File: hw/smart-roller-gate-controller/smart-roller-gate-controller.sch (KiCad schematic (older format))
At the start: 6 parts

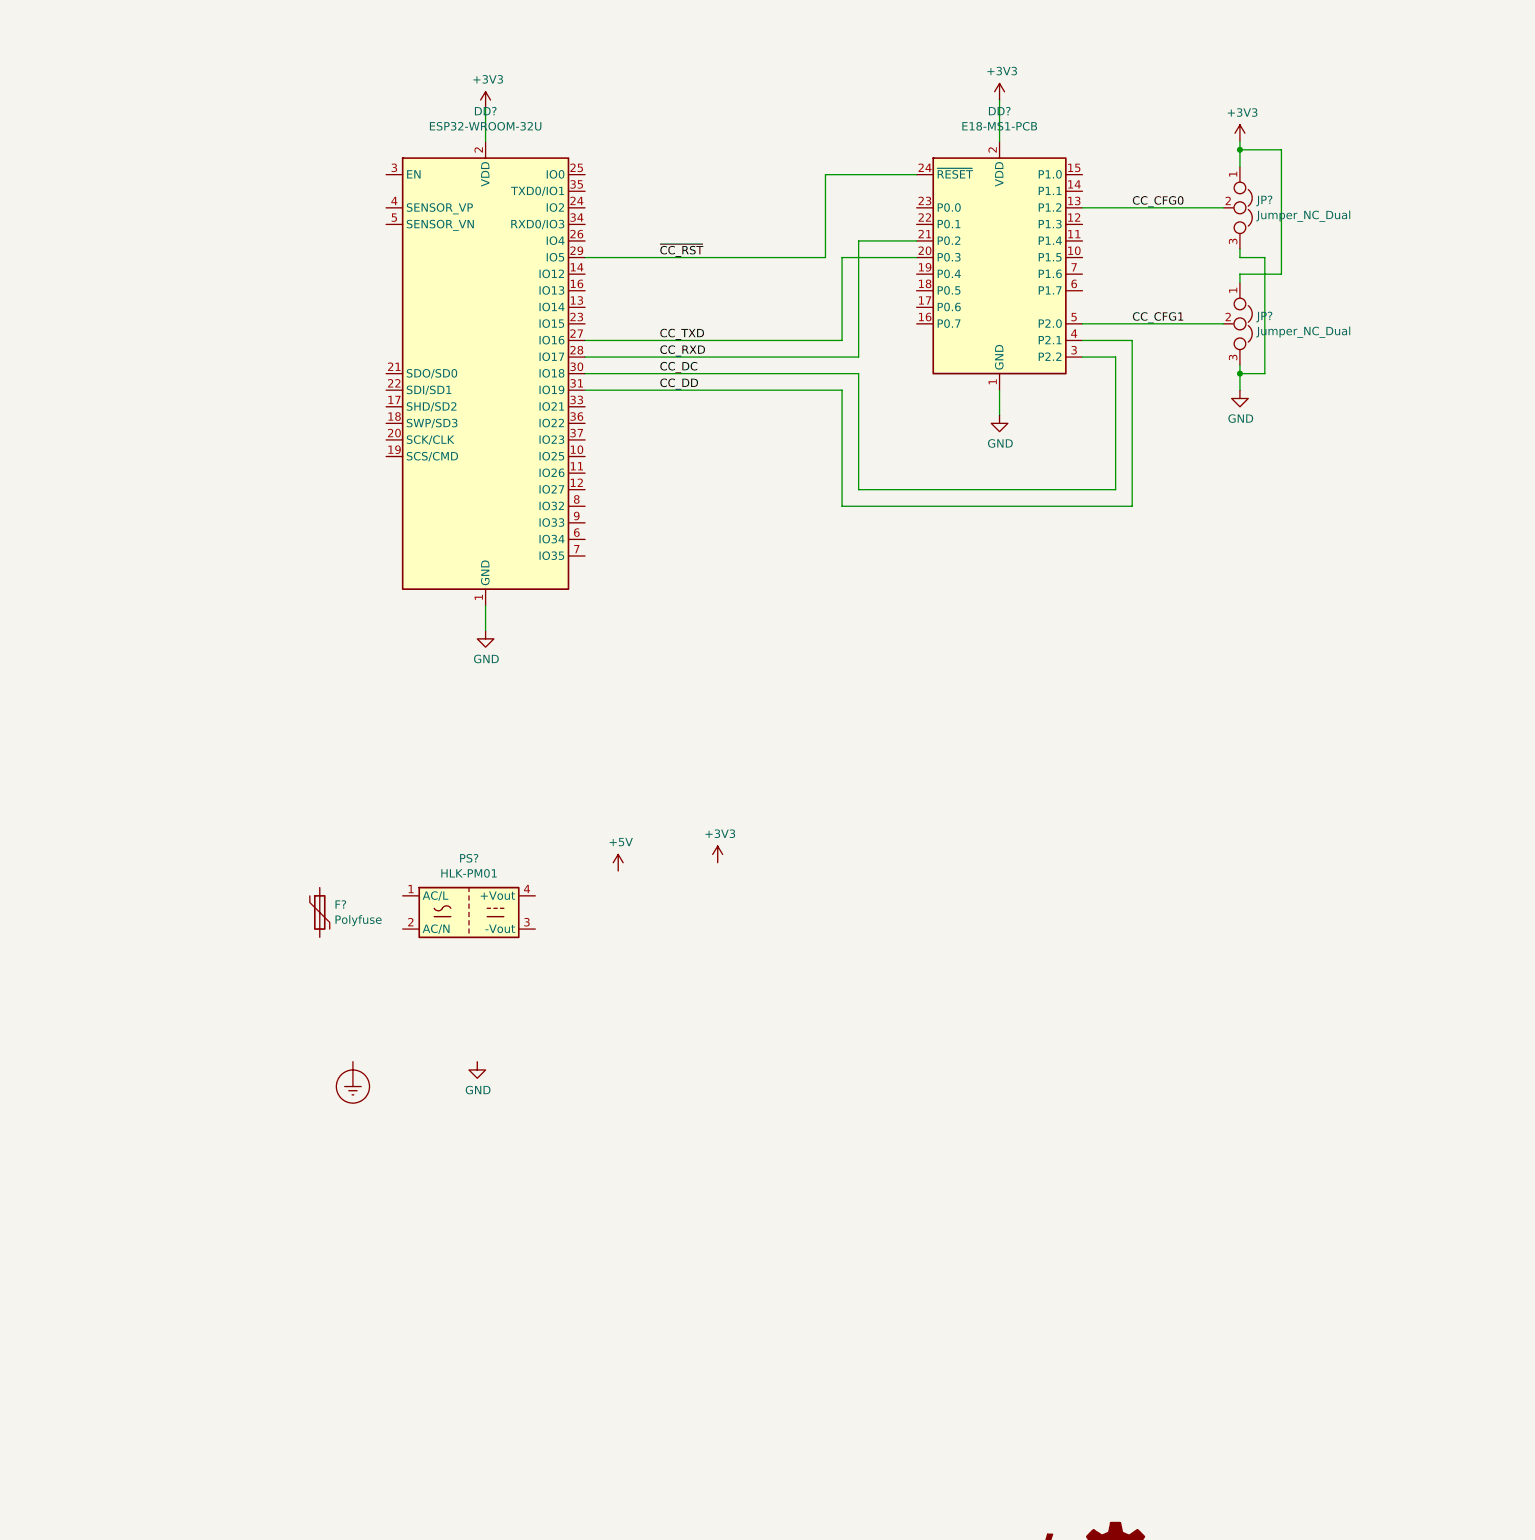
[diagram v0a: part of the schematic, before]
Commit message: hw: HLK-PM01 and HT7333 psu
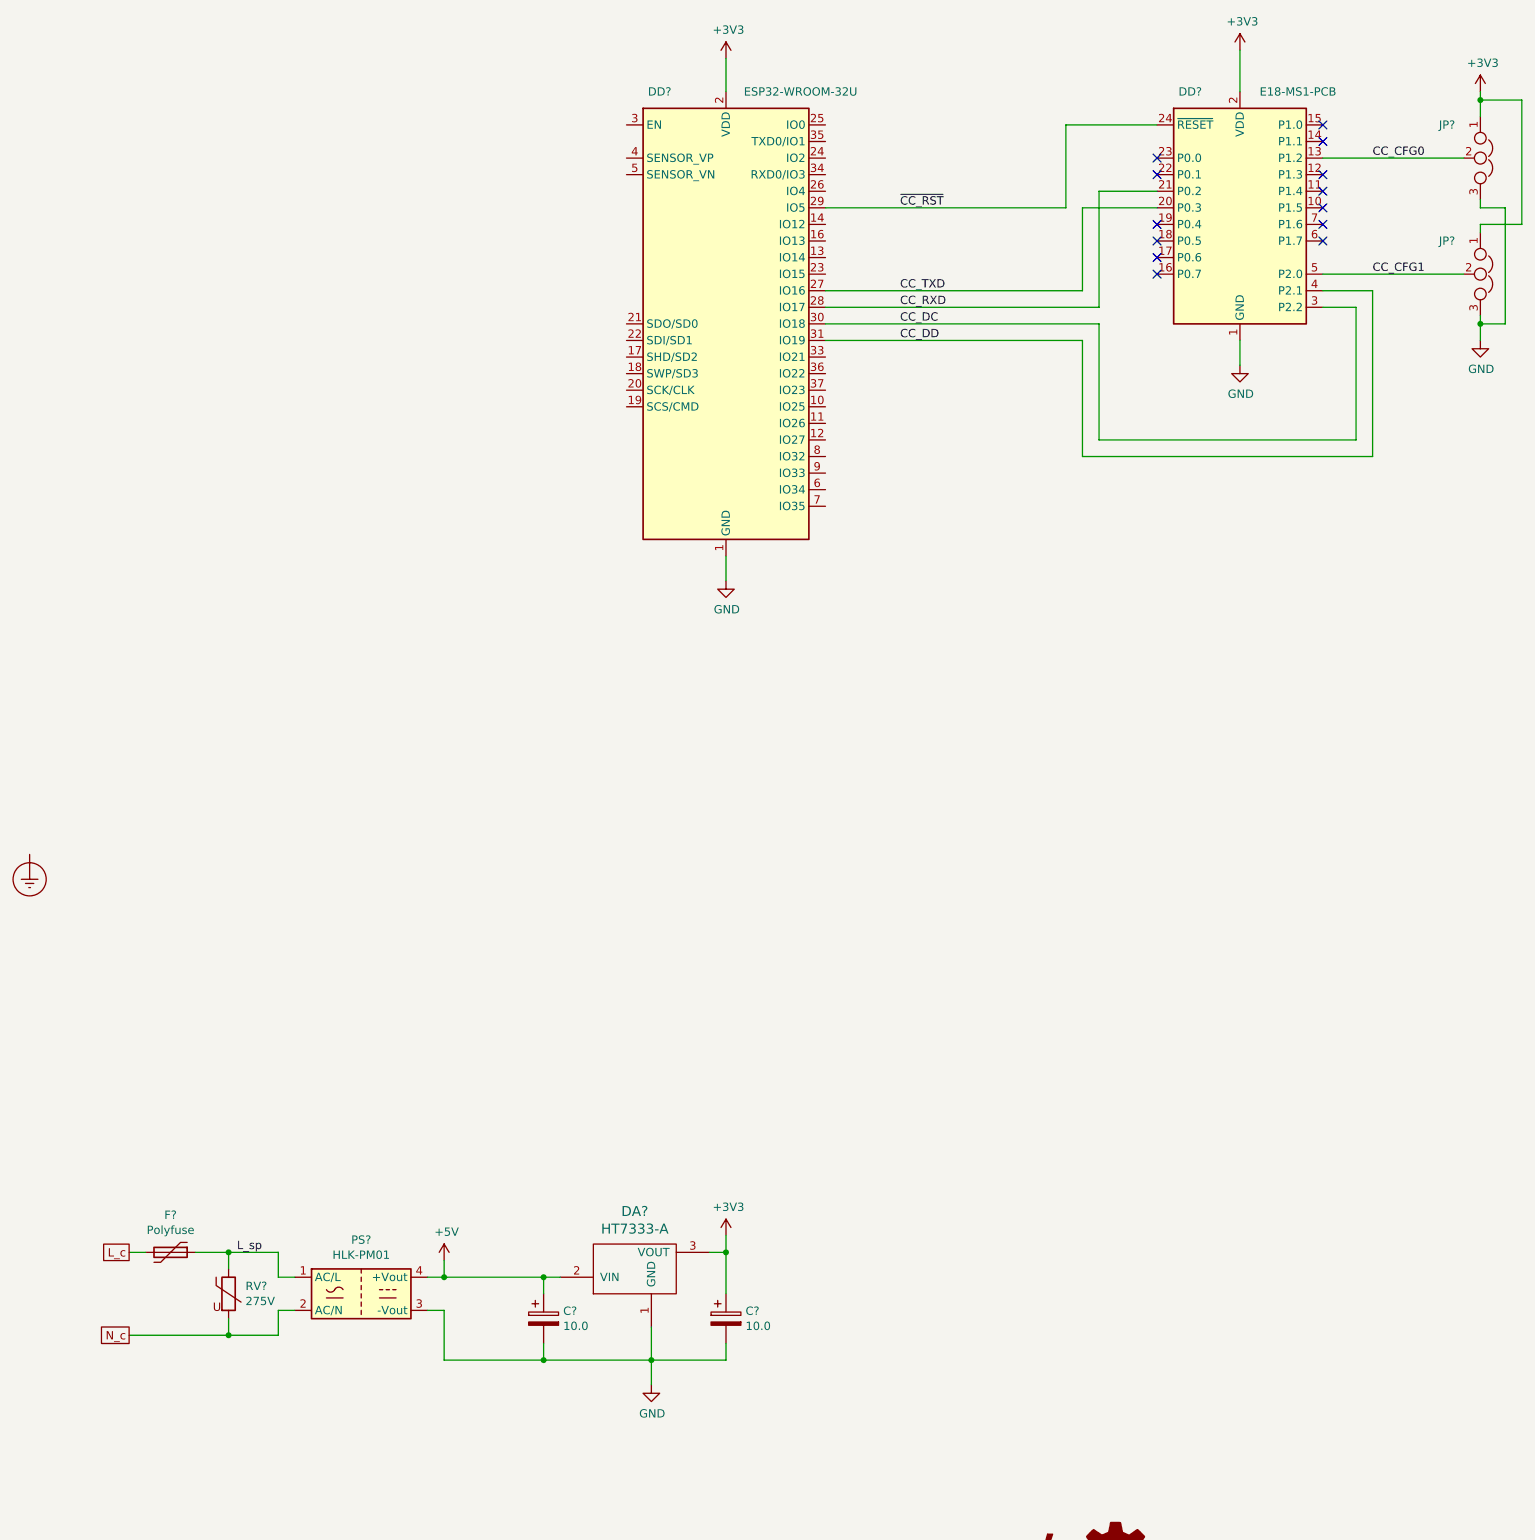
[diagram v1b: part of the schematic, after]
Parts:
- added C? (x2): 10.0, Capacitor_Tantalum_SMD:CP_EIA-3216-10_Kemet-I, symbol Device:CP
- added DA?: HT7333-A, symbol ht7333-a:HT7333-A
- added RV?: 275V, symbol Device:Varistor
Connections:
- net +3V3: now also C?.1, DA?.3 (VOUT)
- net +5V: now also PS?.4 (+Vout), C?.1, DA?.2 (VIN)
- net GND: now also PS?.3 (-Vout), C?.2, C?.2, DA?.1 (GND)
- net L_sp: now reaches PS?.1 (AC/L)
- net L_sp: now also F?.1, RV?.1
- net N_c: now reaches PS?.2 (AC/N)
- net N_c: now also RV?.2
- net L_c: now reaches F?.2
- no-connect marks 0 -> 13
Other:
- moved on the sheet: DD?, F?, JP?, PS?

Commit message: hw: mostly done hv sch
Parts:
- added D? (x2): D, symbol Device:D
- added F? (x2): Polyfuse, symbol Device:Polyfuse
- added K? (x2): PE0, smart-roller-gate-controller:PE014005, symbol rgc_components:PE0
- added R? (x2): R, symbol Device:R
- added XP?: MAINS, symbol Connector:Screw_Terminal_01x04
- added XP? (x2): Screw_Terminal_01x02, Connector_Wire:SolderWirePad_1x02_P5.08mm_Drill1.5mm, symbol Connector:Screw_Terminal_01x02
- added XP?: FENCE SENSOR POWER, symbol Connector:Screw_Terminal_01x04
- added XP?: Conn_01x04, Connector_JST:JST_XH_B4B-XH-A_1x04_P2.50mm_Vertical, symbol Connector_Generic:Conn_01x04
- added XP?: ROLLER MOTOR, symbol Connector:Screw_Terminal_01x04
- added XP?: FENCE INPUTS, symbol Connector:Screw_Terminal_01x04
- added XP?: ROLLER SENSOR, symbol Connector:Screw_Terminal_01x04
- RV?: value 275V -> 440V
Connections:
- net +3V3: now also R?.1, R?.1, XP?.1 (Pin_1)
- net +5V: now also D?.1 (K), D?.1 (K), K?.A1, K?.A1, XP?.1 (Pin_1)
- net Earth_Protective: now also XP?.3 (Pin_3), XP?.4 (Pin_4), XP?.4 (Pin_4)
- net GND: now also XP?.2 (Pin_2), XP?.4 (Pin_4), XP?.4 (Pin_4), XP?.4 (Pin_4)
- net L_c: now also F?.2, F?.2, XP?.1 (Pin_1)
- net N_c: now also XP?.2 (Pin_2), XP?.3 (Pin_3), XP?.3 (Pin_3), XP?.4 (Pin_4)
- net ~RESET: now reaches DD?.3 (EN)
- net ~RESET: now also R?.2
- new net: R?.2, XP?.2 (Pin_2)
- new net BLK1: XP?.1 (Pin_1)
- new net BLK2: XP?.3 (Pin_3)
- new net K1_l: D?.2 (A), K?.A2
- new net K2_l: D?.2 (A), K?.A2
- new net L: XP?.1 (Pin_1), XP?.1 (Pin_1)
- new net L_lock1_2: K?.11, K?.12
- new net L_m: F?.1, K?.11
- new net L_m1: K?.14, XP?.1 (Pin_1)
- new net L_m2: K?.14, XP?.2 (Pin_2)
- new net L_sens: F?.1, XP?.1 (Pin_1), XP?.2 (Pin_2)
- new net N: XP?.2 (Pin_2), XP?.2 (Pin_2)
- new net PZ_RX: XP?.2 (Pin_2)
- new net PZ_TX: XP?.3 (Pin_3)
- no-connect marks 13 -> 14
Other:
- note added: "PZEM-04 Module\n220V 10A"
- moved on the sheet: C?, DA?, F?, PS?, RV?

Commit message: hw: add debug connector
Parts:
- added R? (x3): n/c, symbol Device:R
- added XP?: SOICbite, SOICbite:SOIC_clipProgSmall, symbol Connector_Generic:Conn_02x04_Top_Bottom
- added XP?: SPI, symbol Connector_Generic:Conn_02x05_Odd_Even
- K? (x2): value PE0 -> PE014005
- R?: value R -> 4.7k
- R?: value R -> 10k
- gave numbers to parts that had none: 1
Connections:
- net +3V3: now also R?.1, R?.1, XP?.1 (Pin_1)
- net GND: now also R?.2, XP?.4 (Pin_4)
- net ~RESET: now also XP?.8 (Pin_8)
- net at DD?.23 (IO15): now also R?.2
- net GPIO2: now reaches DD?.24 (IO2)
- net GPIO2: now also R?.1, XP?.3 (Pin_3)
- net GPIO0: now reaches DD?.25 (IO0)
- net GPIO0: now also R?.2, XP?.2 (Pin_2)
- net ESP_RX: now reaches DD?.34 (RXD0/IO3)
- net ESP_RX: now also XP?.5 (Pin_5)
- net ESP_TX: now reaches DD?.35 (TXD0/IO1)
- net ESP_TX: now also XP?.6 (Pin_6)
- net ~RSNS: now reaches R?.2, XP?.2 (Pin_2)
- no-connect marks 14 -> 15
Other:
- note added: "According to datasheet it is not necessary to pull-up/pull-down pins\n\nhttps://www.espressif.com/sites/default/files/documentation/esp32-wroom-32d_esp32-wroom-32u_datasheet_en.pdf"
- moved on the sheet: R?, XP?

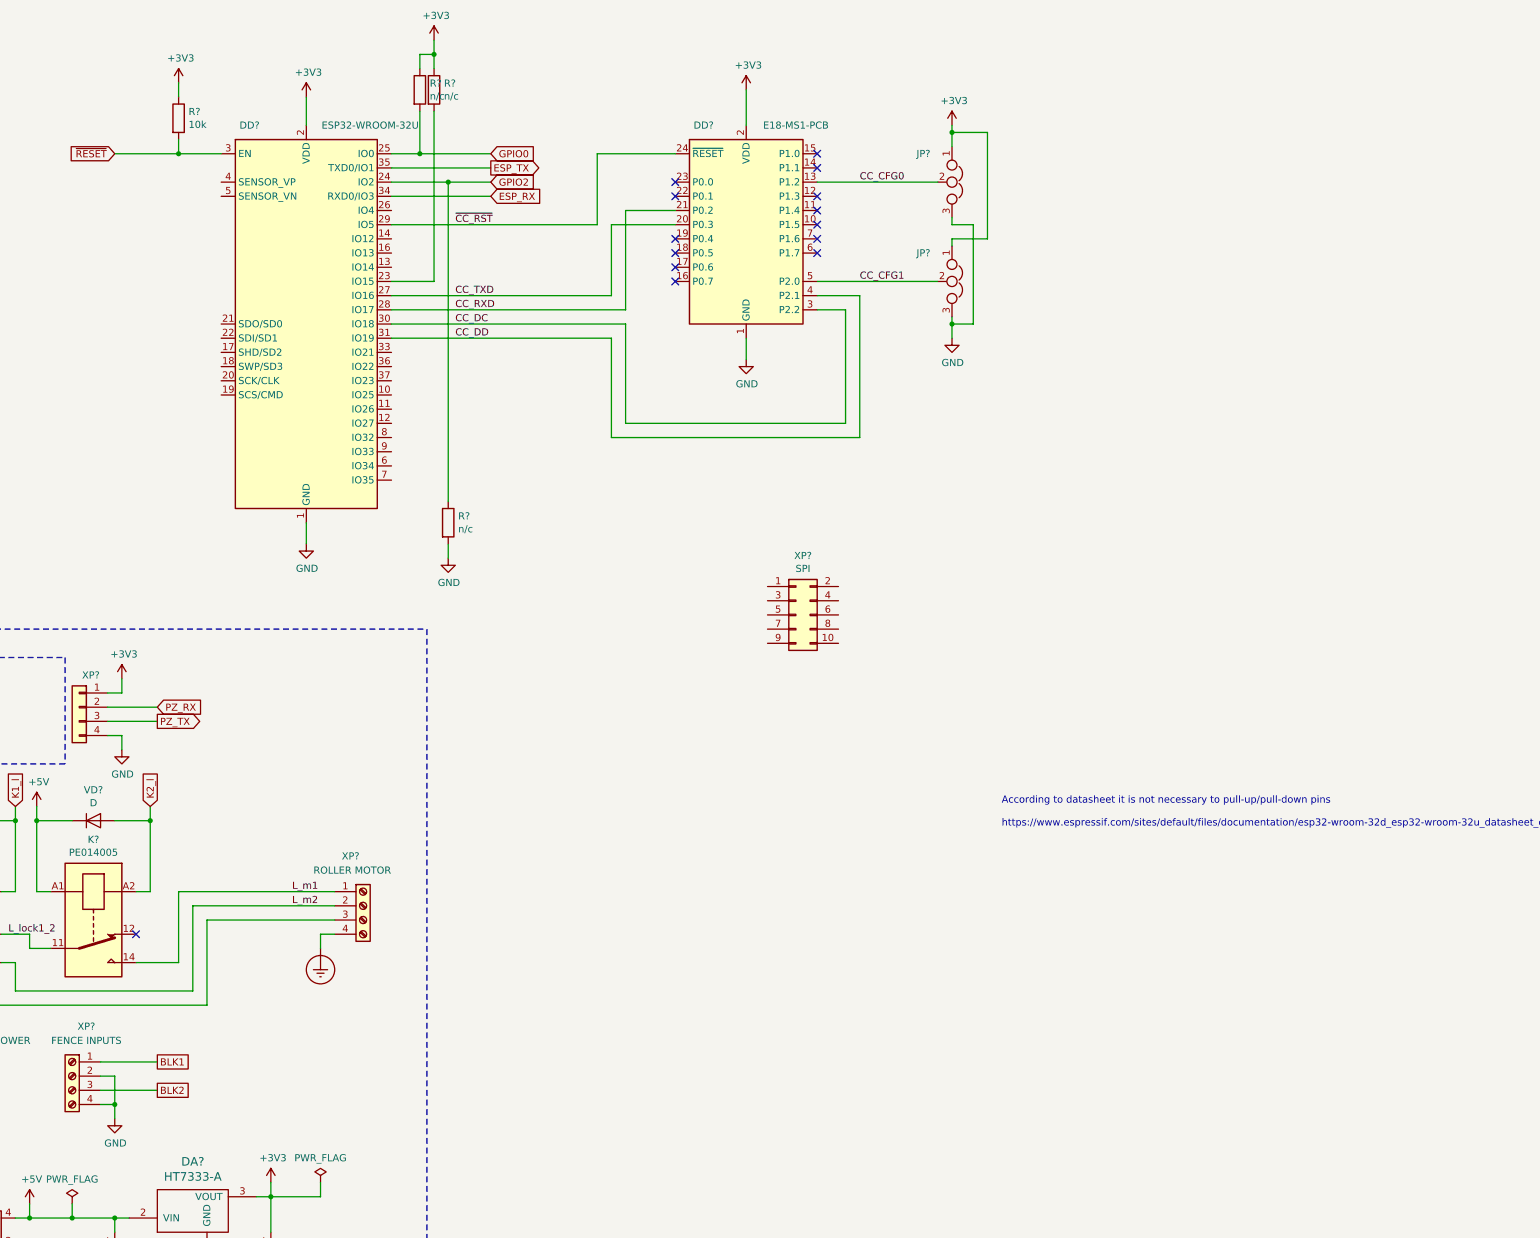
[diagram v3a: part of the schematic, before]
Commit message: hw: connect more patrs
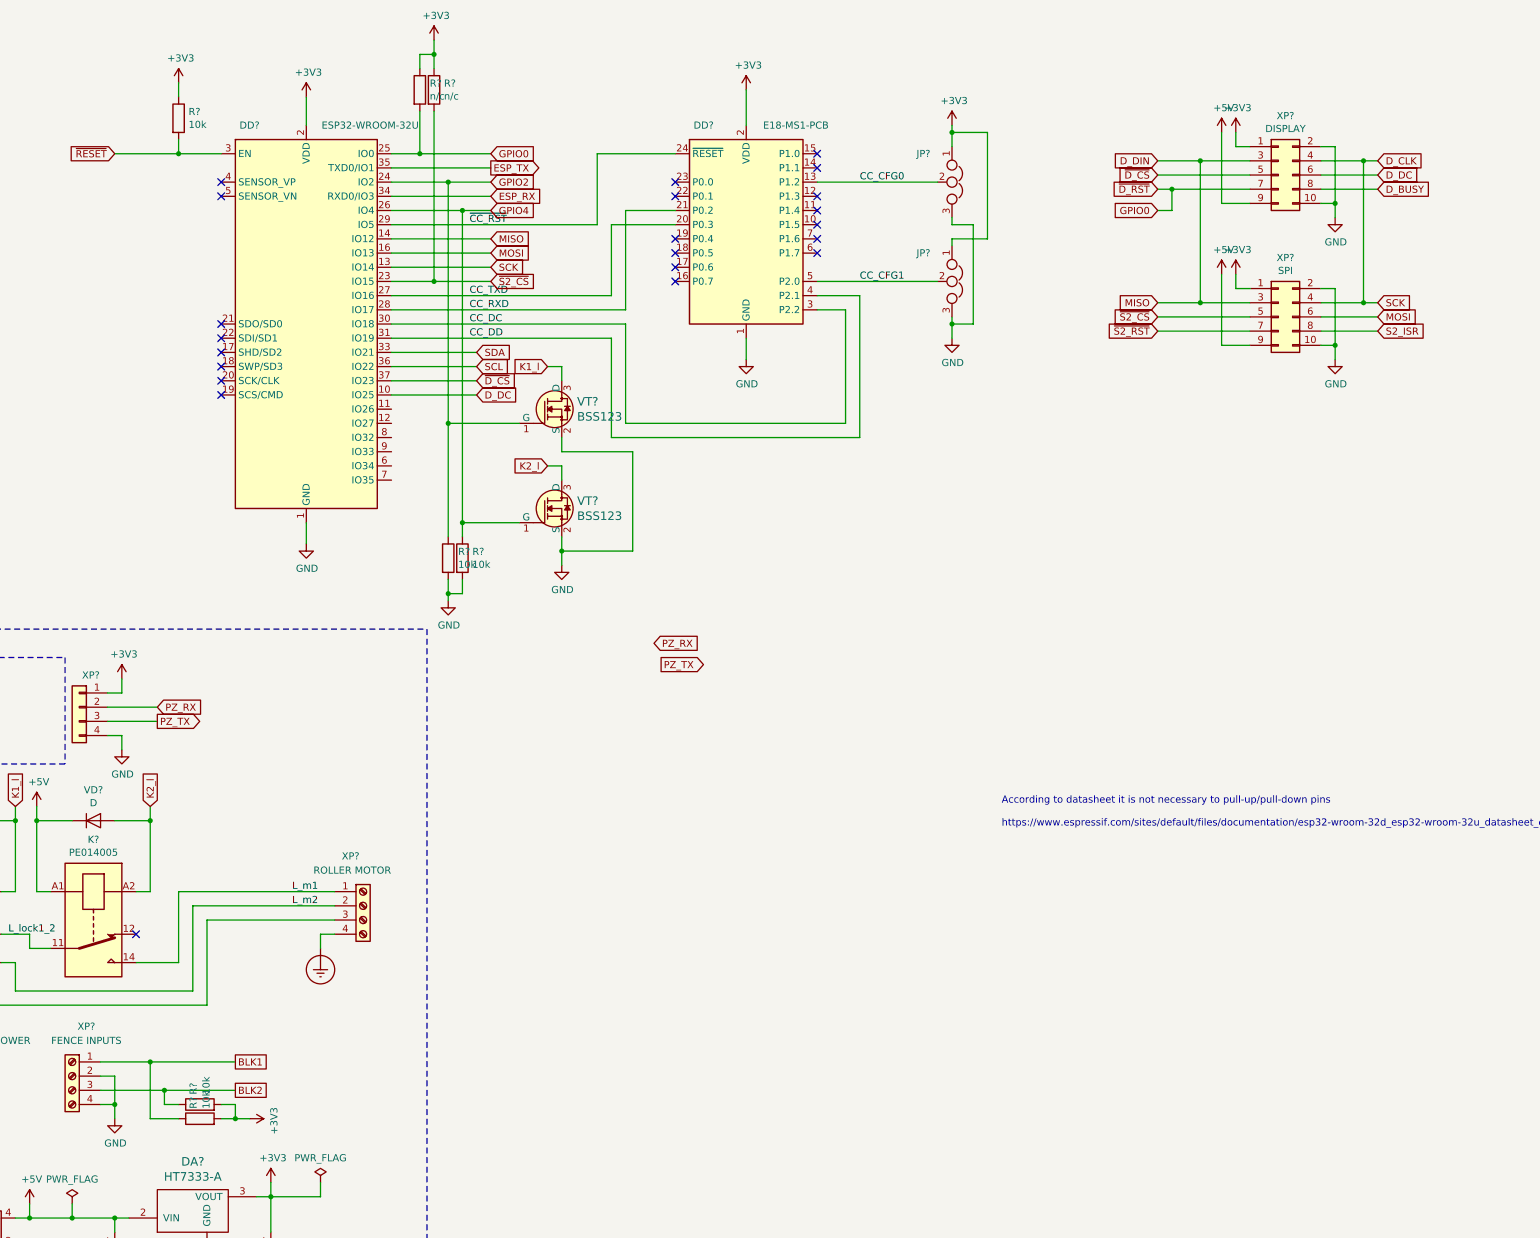
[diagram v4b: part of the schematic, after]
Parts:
- added R? (x3): 10k, symbol Device:R
- added VT? (x2): BSS123, digikey-footprints:SOT-23-3, symbol dk_Transistors-FETs-MOSFETs-Single:BSS123
- added XP?: SPI, smart-roller-gate-controller:CONN-TE-MICROMATCH-5X2-PTH-BOSS, symbol Connector_Generic:Conn_02x05_Odd_Even
- R?: value n/c -> 10k
- XP?: value SPI -> DISPLAY; footprint (none) -> smart-roller-gate-controller:CONN-TE-MICROMATCH-5X2-PTH-BOSS
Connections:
- net +3V3: now also XP?.1 (Pin_1), R?.2, R?.2, XP?.1 (Pin_1)
- net +5V: now also XP?.9 (Pin_9), XP?.9 (Pin_9)
- net BLK1: now also R?.1
- net BLK2: now also R?.1
- net GND: now also XP?.10 (Pin_10), XP?.2 (Pin_2), R?.2, VT?.2 (S), VT?.2 (S), XP?.10 (Pin_10), XP?.2 (Pin_2)
- net GPIO0: now also XP?.7 (Pin_7)
- net GPIO2: now also VT?.1 (G)
- net K1_l: now also VT?.3 (D)
- net K2_l: now also VT?.3 (D)
- net D_DC: now reaches DD?.10 (IO25)
- net D_DC: now also XP?.6 (Pin_6)
- net D_CLK: now reaches DD?.13 (IO14)
- net D_CLK: now also XP?.4 (Pin_4), XP?.4 (Pin_4)
- net D_DIN: now reaches DD?.14 (IO12)
- net D_DIN: now also XP?.3 (Pin_3), XP?.3 (Pin_3)
- net MOSI: now reaches DD?.16 (IO13)
- net MOSI: now also XP?.6 (Pin_6)
- net ~S2_CS: now reaches DD?.23 (IO15), R?.2
- net ~S2_CS: now also XP?.5 (Pin_5)
- net GPIO4: now reaches DD?.26 (IO4)
- net GPIO4: now also R?.1, VT?.1 (G)
- net SDA: now reaches DD?.33 (IO21)
- net SCL: now reaches DD?.36 (IO22)
- net ~D_CS: now reaches DD?.37 (IO23)
- net ~D_CS: now also XP?.5 (Pin_5)
- net D_BUSY: now reaches XP?.8 (Pin_8)
- new net S2_ISR: XP?.8 (Pin_8)
- new net ~S2_RST: XP?.7 (Pin_7)
- no-connect marks 15 -> 23
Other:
- moved on the sheet: R?, XP?
